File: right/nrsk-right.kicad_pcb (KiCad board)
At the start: 2 copper layers, 199.6 x 133.6 mm, 145 parts, among them J1 PJ-320D, J2 USB-C, J3 OLED 128x32, SW1 71, SW10 8, SW11 9, SW12 0, SW13 -, SW14 =, SW15 Backspace, SW16 75, SW17 Y, SW18 U, SW19 I, SW2 F7, SW20 O, SW21 P, SW22 [, SW23 ], SW24 \, SW25 77, SW26 H, SW27 J, SW28 K, SW29 L, SW3 F8, SW30 ;, SW31 ', SW32 Enter, SW33 79, SW34 N, SW35 M, SW36 ,, SW37 ., SW38 /, SW39 ↑, SW4 F9, SW40 fn, SW41 81, SW42 Space, SW43 Space, SW44 Cmd, SW45 Opt, SW46 ←, SW47 ↓, SW48 →, SW5 F10, SW6 F11, SW7 F12, SW8 73, SW9 7, U1 RP2040, U2 USBLC6-2SC6, U4 AP2112K-3.3, U5 W25Q128JVS, Y1 12MHz

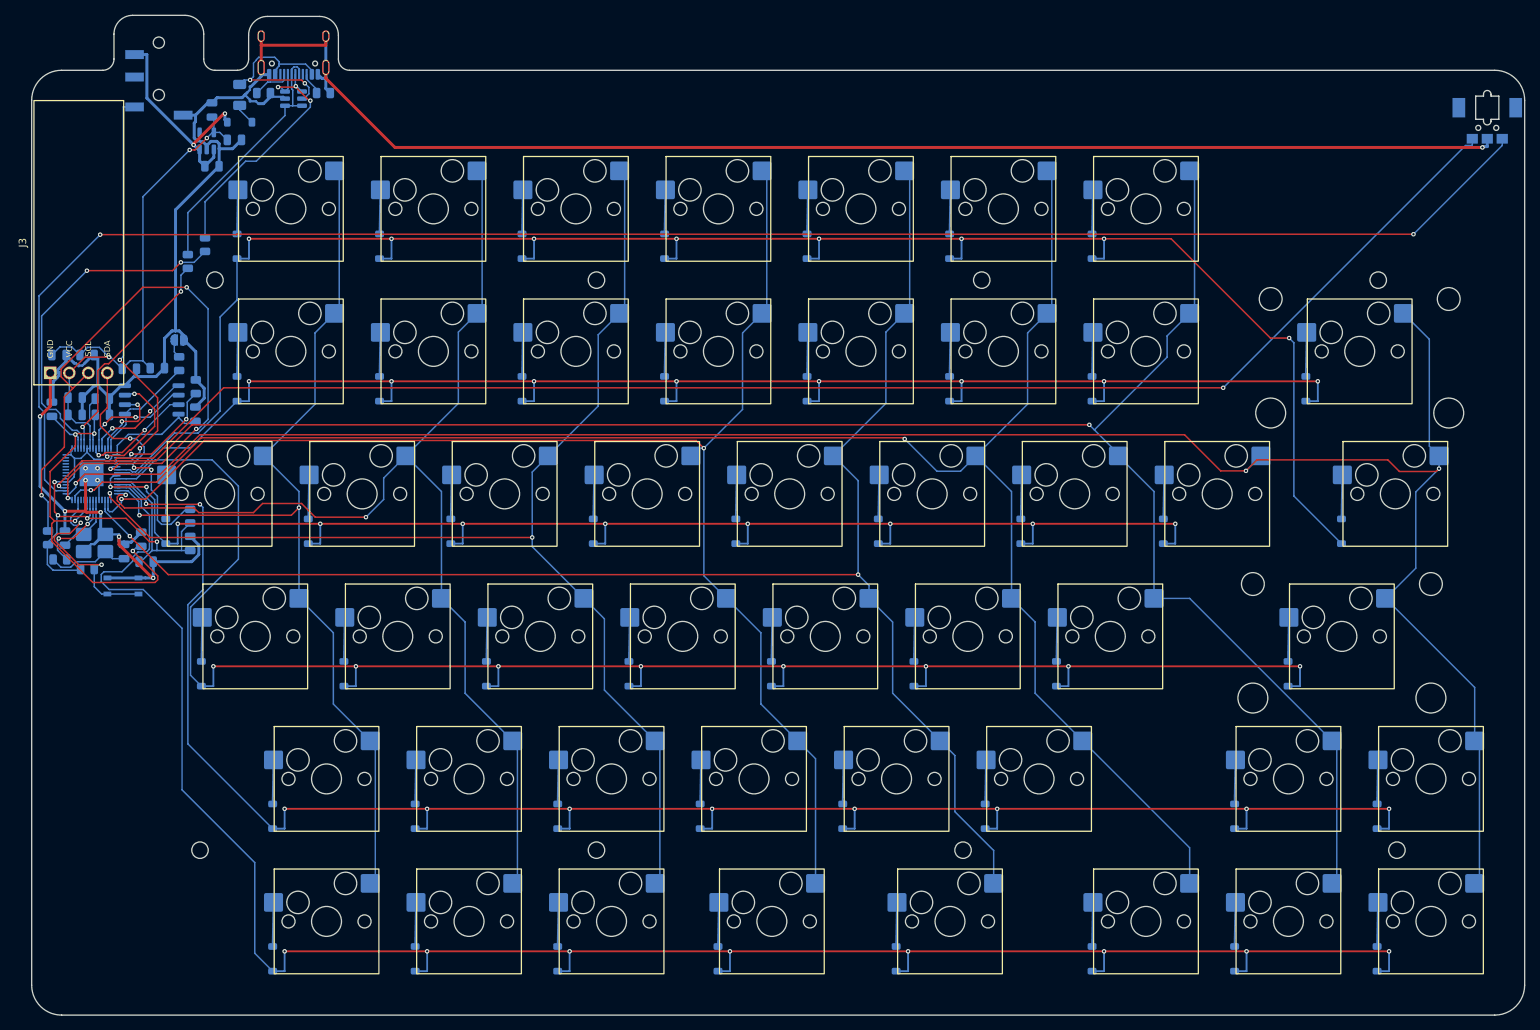
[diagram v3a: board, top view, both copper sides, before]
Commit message: GND copper on both faces of both boards, stitched with vias
- route.py pour(), run after routing and cleanup: a GND zone over the whole board on F.Cu and B.Cu
  (0.3 mm to other nets, 0.25 mm minimum width; the mounting-hole keepouts still win). The routed
  GND tracks stay. SMD pads join solidly (JLC reflows them), through-hole pads get thermal spokes,
  except the USB-C shell legs (JLC solders them; solid to GND)
- Stitching vias (0.6 / 0.3 mm) on a 5 mm grid, plus a 1.25 mm grid wherever no via is within
  3.75 mm, so narrow copper boxed in by tracks gets one too; a via goes only where its ring lies in
  the copper of both faces and its drill keeps 0.5 mm from other holes. Islands still unconnected are
  removed, with any via standing in them. Left 850, right ~966 stitching vias
- Applied to the routed boards (placement and routing unchanged, so the JLC CPL is unchanged);
  future builds pour after each routing pass
- DRC: 5 per side (silk at the connector mouths), down from 8: the 3 RP2040 thermal-pad vias now
  reach the F.Cu copper. 0 unconnected, 0 parity issues, ERC 0. Gerbers, PDFs, 3D viewer, assembly
  guide and board images regenerated
- README: board spec, how the copper is poured, DRC note

Co-Authored-By: Claude Opus 5.5 <noreply@anthropic.com>
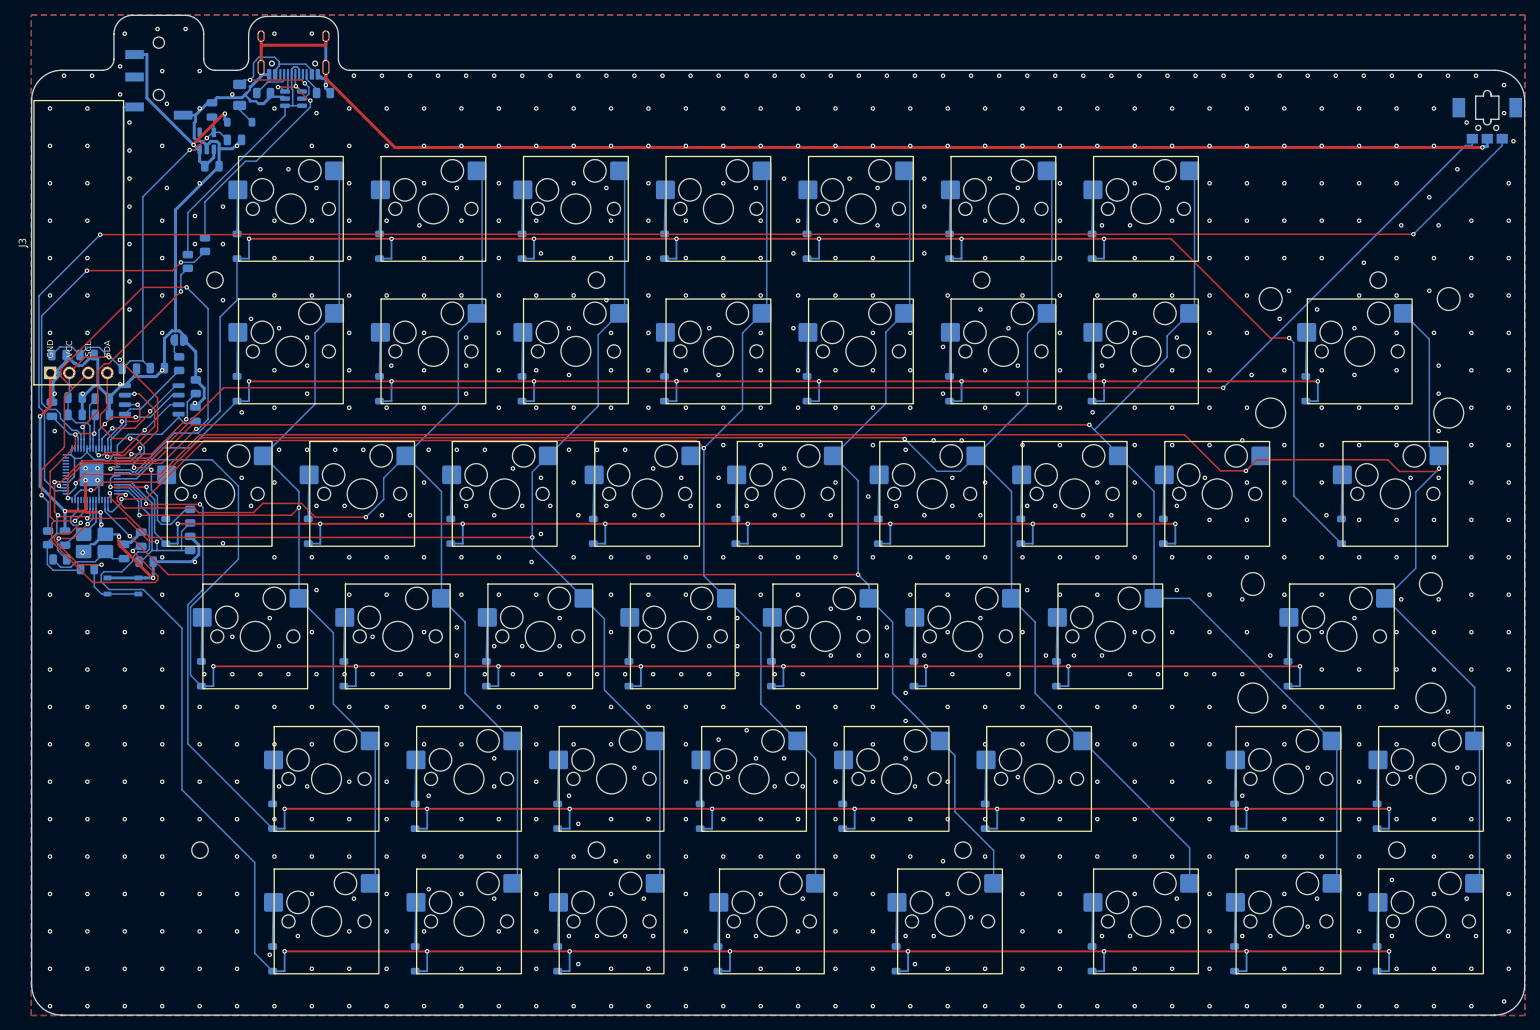
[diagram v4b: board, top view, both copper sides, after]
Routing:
- net GND: vias 10 -> 975
- added copper zone on B.Cu, net GND
- added copper zone on F.Cu, net GND

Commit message: Drum dial step 3: EC10E and the bearing-block holes on the right board
make_pcb.py places ENC2 on the front with its shaft-insert face 17.15 mm right of the F12 key centre, on
that key's row, so the encoder stays tied to the top row if the layout moves. Next to it goes
Drum_Dial_Bearing, a board-only footprint with the two 2.0 mm NPTH for the printed block's pegs and a
courtyard over the drum and block, so the automatic mounting holes and parts stay out of that area (the
top-right hole moved from x 177.0 to 180.0). The drum origin and peg holes go into case_data.json for the
case generator. The EC10E's leg pads shrink by 0.1 mm to keep 0.15 mm from terminal A.

Checked: ./build.sh right -> 0 unconnected, 0 schematic parity issues, ERC 0; DRC has only the 5 existing
silkscreen-at-board-edge warnings (J1 / J2), same as before.

Co-Authored-By: Claude Opus 5.5 <noreply@anthropic.com>
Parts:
- added DRUM1: Drum_Dial_Bearing, nrsk:Drum_Dial_Bearing, F.Cu at (193.1, 39.5)
- added ENC2: EC10E1220505, nrsk:Alps_EC10E, F.Cu at (193.1, 39.5)
- moved H4 3.00 mm to (210.0, 49.0)
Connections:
- U1 pad 34: unconnected-(U1-GPIO22-Pad34) -> /DRUM_A
- U1 pad 35: unconnected-(U1-GPIO23-Pad35) -> /DRUM_B
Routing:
- net /DRUM_A: track 0.00 -> 191.9 mm, vias 0 -> 1
- net /DRUM_B: track 0.00 -> 175.9 mm, vias 0 -> 2
- net /3V3: track 167.0 -> 219.5 mm, vias 7 -> 2
- net /SCL: track 84.3 -> 53.5 mm, vias 4 -> 2
- net /QSPI_SD1: track 10.7 -> 38.2 mm, vias 2 -> 4
- net /ENC_B: track 209.9 -> 224.2 mm
- net /SDA: track 35.0 -> 49.0 mm, vias 3 -> 1
- net /DATA: track 54.4 -> 65.9 mm
- net /D+: track 30.3 -> 41.8 mm, vias 2 -> 4
- net /ROW5: track 265.9 -> 256.1 mm, vias 8 -> 10
- net GND: track 379.5 -> 371.4 mm, vias 975 -> 970
- net /QSPI_SD2: track 16.4 -> 8.55 mm, vias 2 -> 0
- net /ROW3: track 227.9 -> 220.3 mm, vias 8 -> 10
- net /COL6: track 261.3 -> 268.7 mm
- net /RUN: track 27.3 -> 20.5 mm, vias 2 -> 3
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
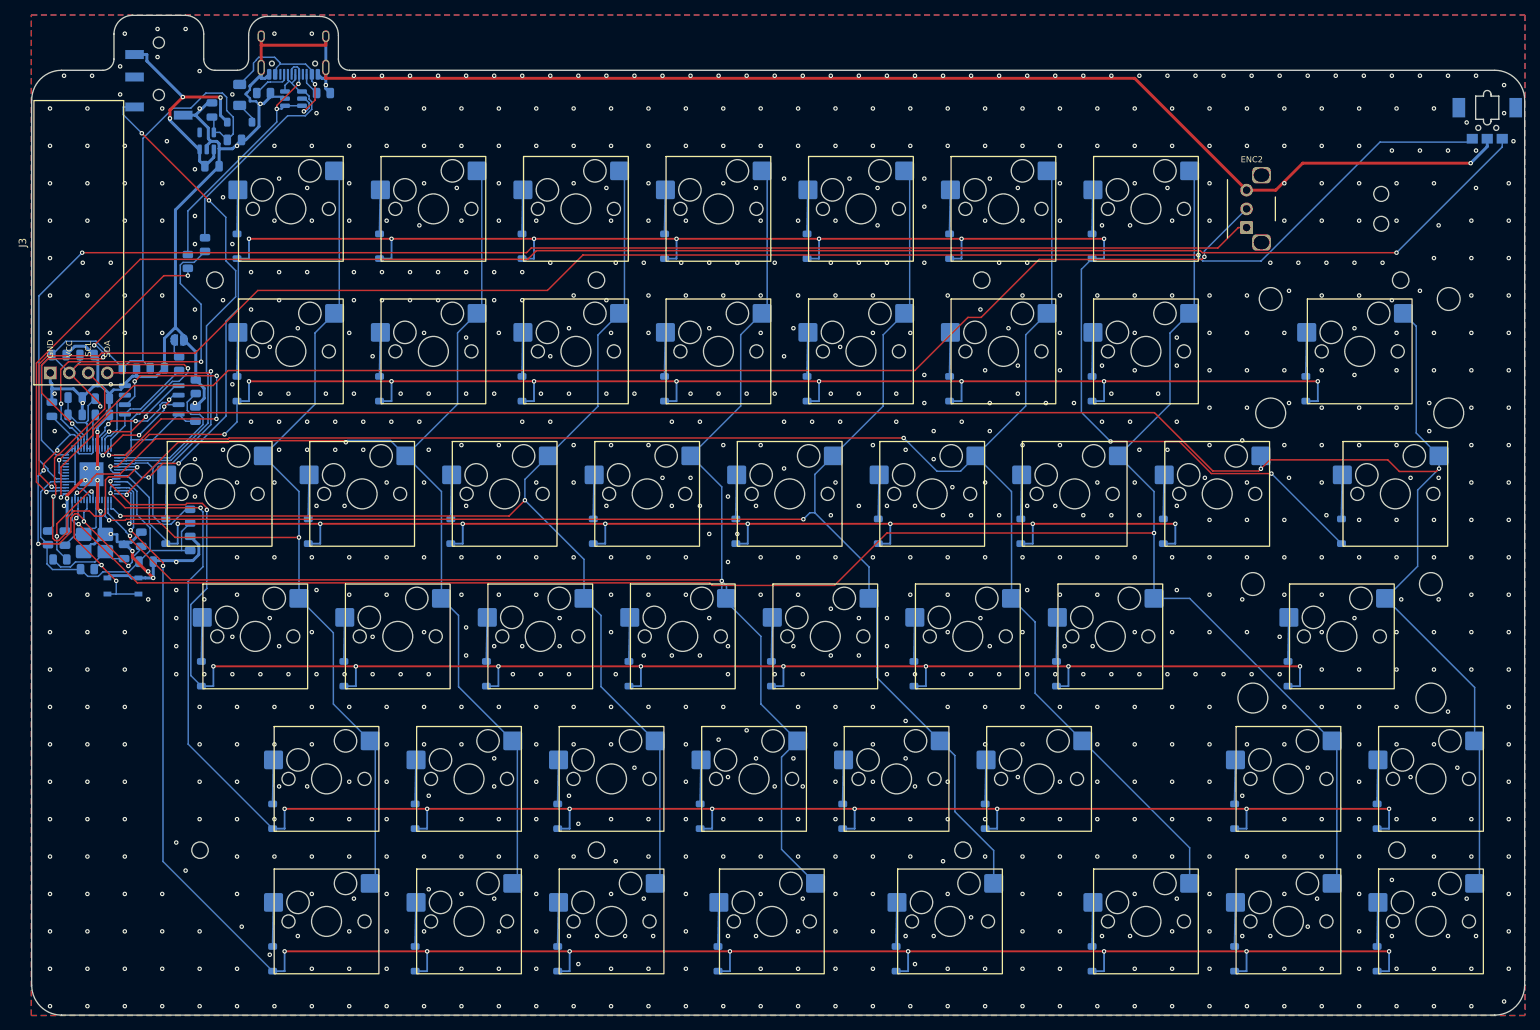
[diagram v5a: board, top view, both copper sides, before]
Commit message: Drum dial: centre the drum on Backspace
The drum's centre now lines up with the 2 u Backspace below it (x 174.5): SIDES['right']['drum'] takes the
x from Backspace and the row from F12, so the place stays tied to those keys when the layout changes. The
encoder sits at x 162.0-168.1 and the bearing block at 180.9-183.9, over the thumbwheel under the board;
the block's pegs stop inside the 1.6 mm board, and the encoder's terminals stay outside the wheel. The
top-right mounting hole moved to (168.0, 19.05), outside the plate opening.

The spec records the new place and what changed while implementing: the encoder hood is open toward the
drum, a second hood holds the bearing block down instead of an arm, the opening is +/-7.6 mm deep for the
hooks, the hex pin stands 3.3 mm out of the drum (1.6 mm in the rotor), the EC10E is hand-soldered, and
qmk compile is still to be run.

Checked: ./build.sh right -> routing try 2: 0 unconnected, ERC 0, parity 0, DRC only the 5 existing
silkscreen warnings; make_case.py -> "right drum dial checks ok".

Co-Authored-By: Claude Opus 5.5 <noreply@anthropic.com>
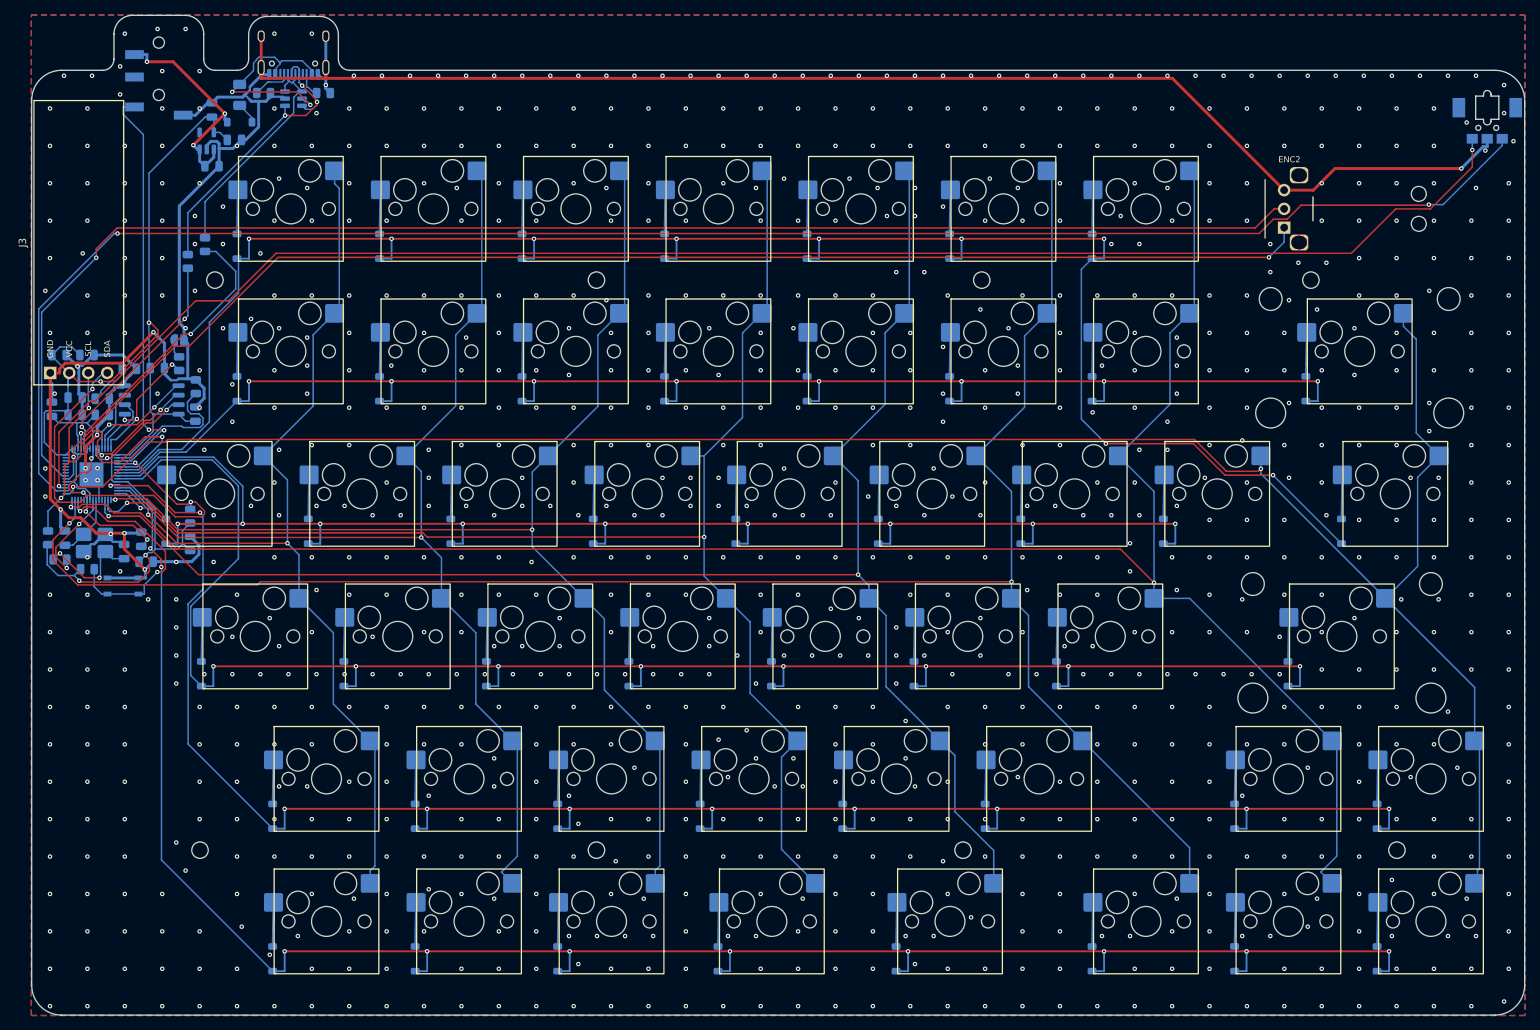
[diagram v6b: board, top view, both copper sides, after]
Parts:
- moved H4 12.0 mm to (198.0, 49.0)
- moved DRUM1 5.03 mm to (198.1, 39.5)
- moved ENC2 5.03 mm to (198.1, 39.5)
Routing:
- net /3V3: track 219.5 -> 176.6 mm, vias 2 -> 4
- net GND: track 371.4 -> 401.9 mm, vias 970 -> 956
- net /QSPI_SD1: track 38.2 -> 8.14 mm, vias 4 -> 0
- net /ROW2: track 179.9 -> 200.5 mm, vias 8 -> 9
- net /DRUM_B: track 175.9 -> 196.0 mm, vias 2 -> 1
- net /1V1: track 54.5 -> 37.0 mm, vias 5 -> 4
- net /DRUM_A: track 191.9 -> 180.0 mm, vias 1 -> 2
- net /RUN: track 20.5 -> 32.4 mm, vias 3 -> 2
- net /COL5: track 238.6 -> 250.5 mm
- net /D+: track 41.8 -> 30.2 mm, vias 4 -> 2
- net /D-: track 49.2 -> 38.3 mm
- net /DATA: track 65.9 -> 56.1 mm
- net /SDA: track 49.0 -> 58.0 mm, vias 1 -> 3
- net /ENC_B: track 224.2 -> 215.6 mm
- net /COL7: track 285.5 -> 277.5 mm, vias 3 -> 2
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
